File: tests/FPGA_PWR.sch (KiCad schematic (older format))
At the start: 42 parts, among them U4 iCE40-HX8K-CT256, U8 AZ1117EH-ADJ

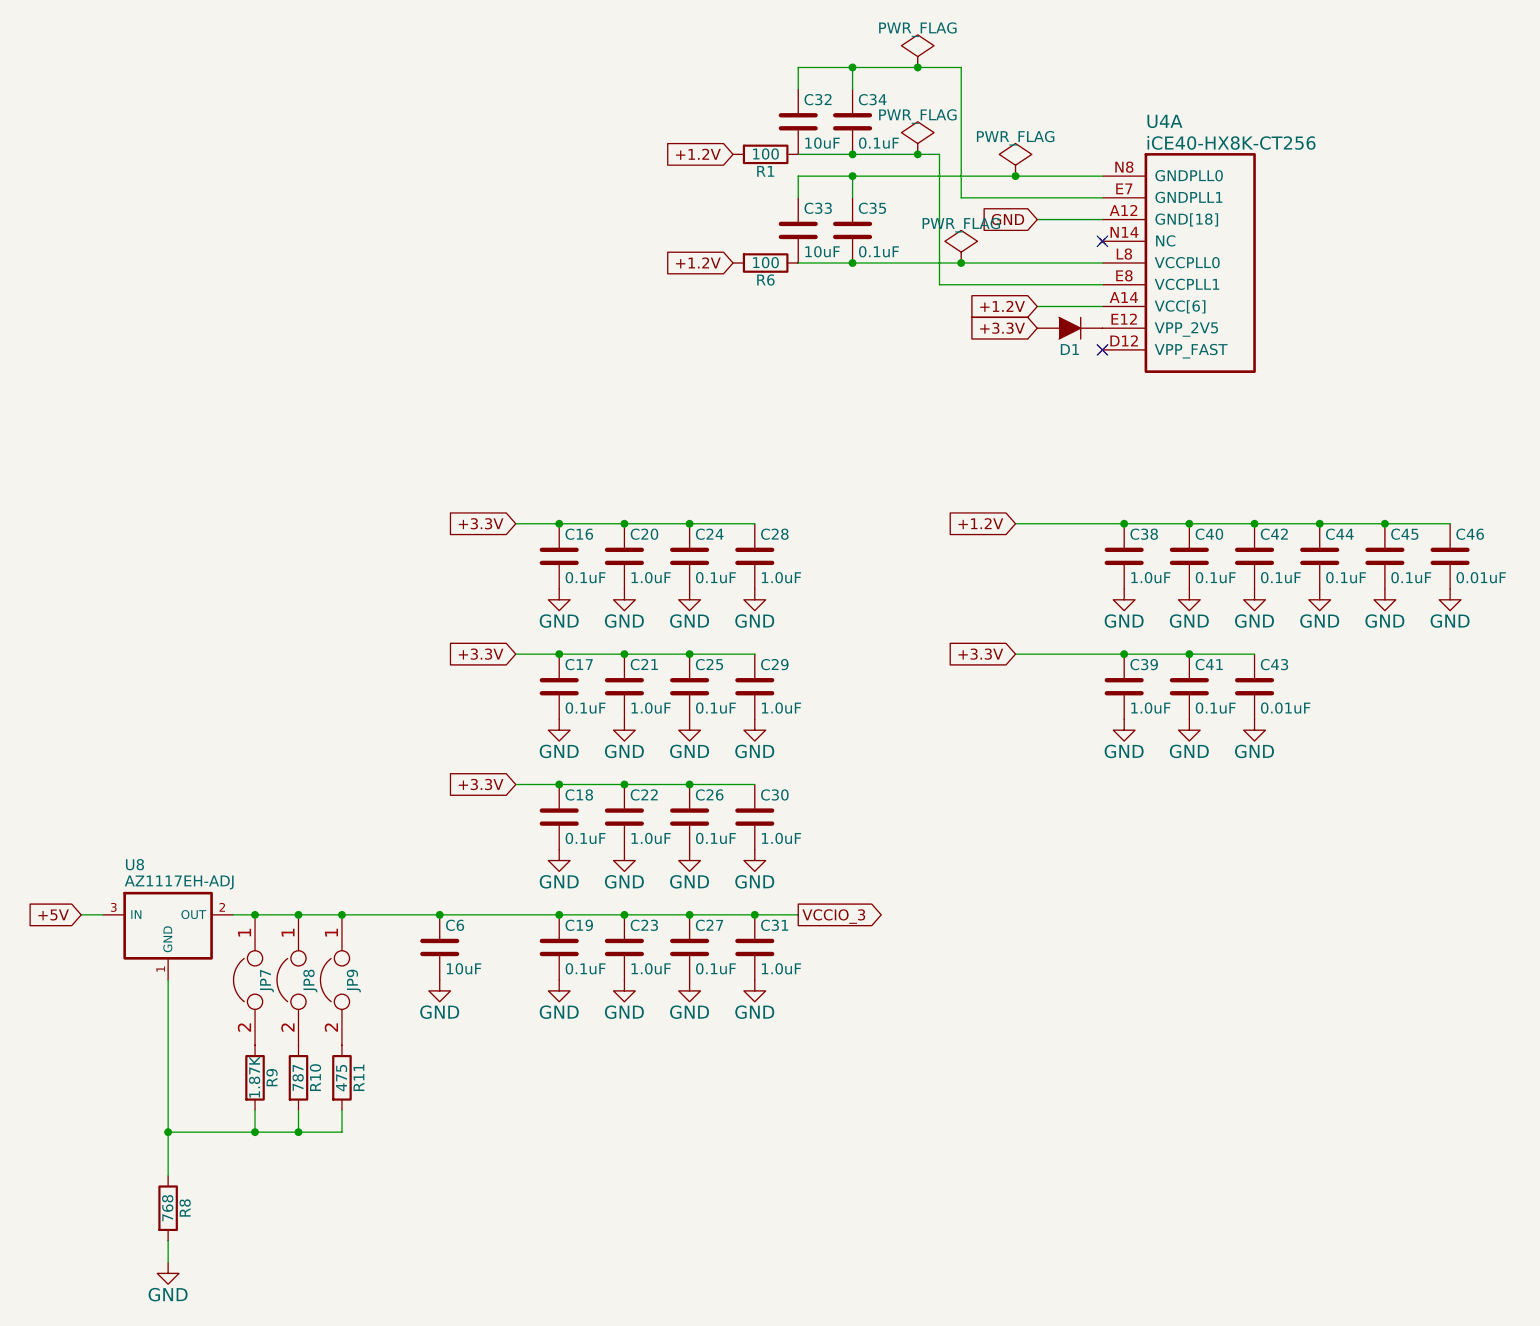
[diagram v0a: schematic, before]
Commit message: Added recursive operations on hierarchical schematics.
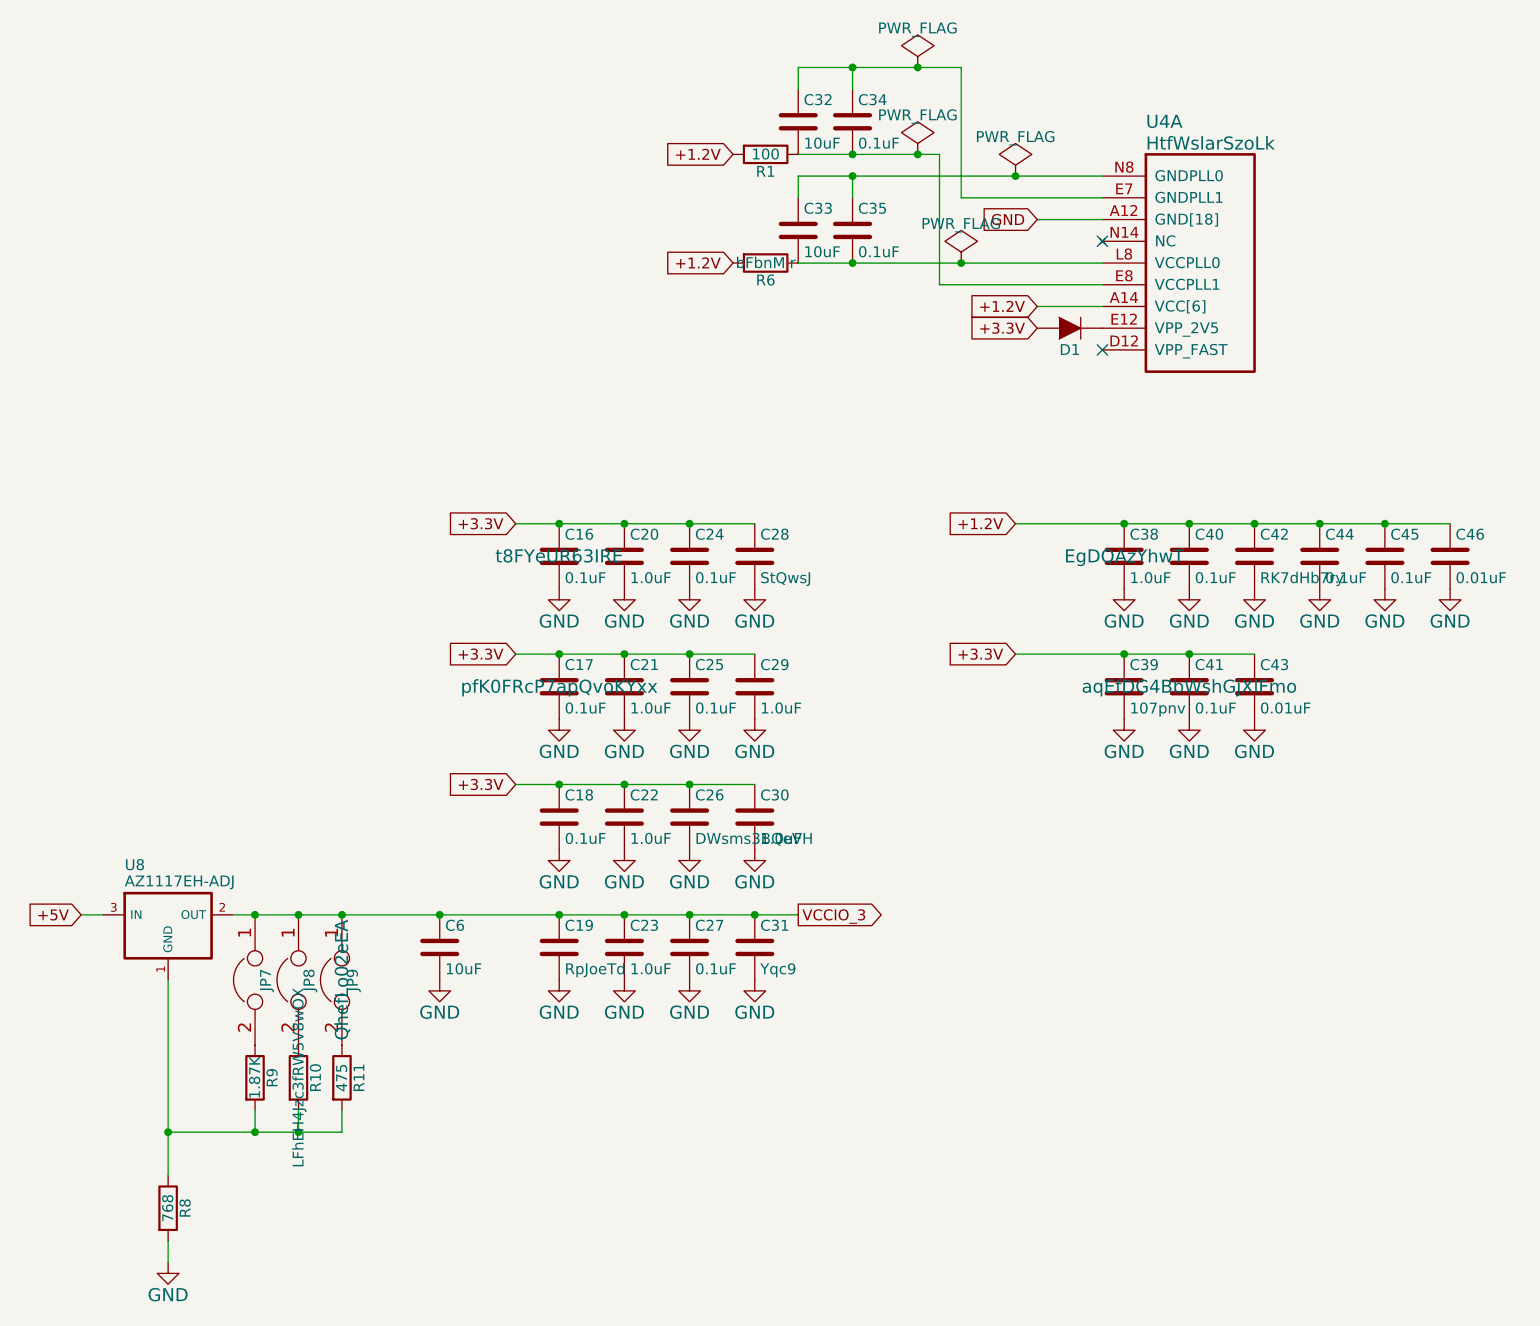
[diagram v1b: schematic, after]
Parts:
- C16: footprint Capacitors_SMD:C_0603 -> VPseWLMK4CuWKZj
- C17: manf# (none) -> ZXw31Fcg
- C18: zzzky (none) -> bqwA6pG1NpEs7hVg6pI
- C19: value 0.1uF -> RpJoeTd; zzzDXp9J5Qc (none) -> 5vpqd6McjV4FjLGdu
- C20: zzzkoq (none) -> Mt97z
- C21: zzzkoq (none) -> VjlRVcaG48JSVPDr
- C23: zzz4ozZ3f (none) -> myT7Til3rlujmnheu
- C24: footprint Capacitors_SMD:C_0603 -> O0F2jcxKZsY2; manf (none) -> im4msh
- C25: footprint Capacitors_SMD:C_0603 -> tLrB4oo; manf# (none) -> QVSM; zzz9xP (none) -> p5udih; zzzDXp9J5Qc (none) -> a8yfFgOdMdpA
- C26: value 0.1uF -> DWsms3BQeVH; footprint Capacitors_SMD:C_0603 -> x5qdQJUBLuL8kbk; manf (none) -> eCxzP849bQJ3VHl3ivP
- C27: zzzkoq (none) -> oc1eDwaLHAJpbfQ3
- C28: value 1.0uF -> StQwsJ; manf (none) -> g0icGWhKkoY6TggPORT; zzz9xP (none) -> h5j3zLdDWpj2d
- C29: zzz4ozZ3f (none) -> QGaXLdXjex
- C30: zzzky (none) -> WUaQxf54OuOBeulF69
- C31: value 1.0uF -> Yqc9; zzz4ozZ3f (none) -> Lgh2N0k39PmMOgAsTH
- C32: manf (none) -> YTcqd1XAjs40F; zzz4ozZ3f (none) -> 9Ts6n8eQrt
- C33: footprint Capacitors_SMD:C_0805 -> k1rid; manf (none) -> OvaFJwLYohgGmdia9Gm
- C35: zzz9xP (none) -> UWNBe6eFfyqbuWTkfvm
- C38: zzz9xP (none) -> ub4Rz
- C39: value 1.0uF -> 107pnv
- C40: manf# (none) -> zOQb50K
- C41: manf (none) -> S5lxzP9C2SgF0tq; manf# (none) -> N75aFU9A4aKkrcY
- C42: value 0.1uF -> RK7dHb7ry; manf (none) -> hItCMxO; manf# (none) -> NNpNDS
- C43: zzz9xP (none) -> Q66oaMC5zrYs
- C44: zzz4ozZ3f (none) -> lOkC; zzz5 (none) -> E0ge0lb04BaJoeN; zzzky (none) -> 9KG8VM1a0vpI6tMYzA
- C45: manf (none) -> fGUigpBr; zzz5 (none) -> qIyCsRTLnBWN8NxOBtm; zzzDXp9J5Qc (none) -> tapoaEchrbffcm4Qph
- C46: footprint Capacitors_SMD:C_0603 -> w8qzJDIl; zzz5 (none) -> Dro0kCenJOVT45En15
- C6: zzz5 (none) -> hXzqJNKHTHWI
- JP7: value JUMPER -> QuI32; manf# (none) -> H2gyBXidmdrO; zzz5 (none) -> Lg7FM
- JP8: value JUMPER -> NoSBuD36qdzSyq; zzzkoq (none) -> ZiBg5ETPwZmkwf3h9A
- JP9: footprint XESS:S_JUMPER_2 -> V4rn0mPDog; zzz4ozZ3f (none) -> VEro8sjz3luO
- R10: value 787 -> LFhEH4Jzc3fRW5V8wOX; footprint Resistors_SMD:R_0603 -> 01YvrugDO1jjAGyYIm; manf (none) -> 8G49xHT; zzzky (none) -> gOmo
- R11: zzz5 (none) -> cYXiLdtnD
- R6: value 100 -> bFbnMlr; zzzkoq (none) -> yokSKrMTxGpjBIcTX
- R8: manf# RC0603FR-07768RL -> cRyXLfRDmVWyKdp; zzz9xP (none) -> 4FefrDttC8lAVGdv
- R9: zzzkoq (none) -> JxtfrnEHpG3CHkK
- U4: value iCE40-HX8K-CT256 -> HtfWslarSzoLk; manf# ICE40HX8K-CT256 -> HiyQG6ncOK
